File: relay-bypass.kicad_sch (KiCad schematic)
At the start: 39 parts, among them J2 8, K1 IM05JR, Q1 DMN62D0U-7, U1 STM32C011F4Ux

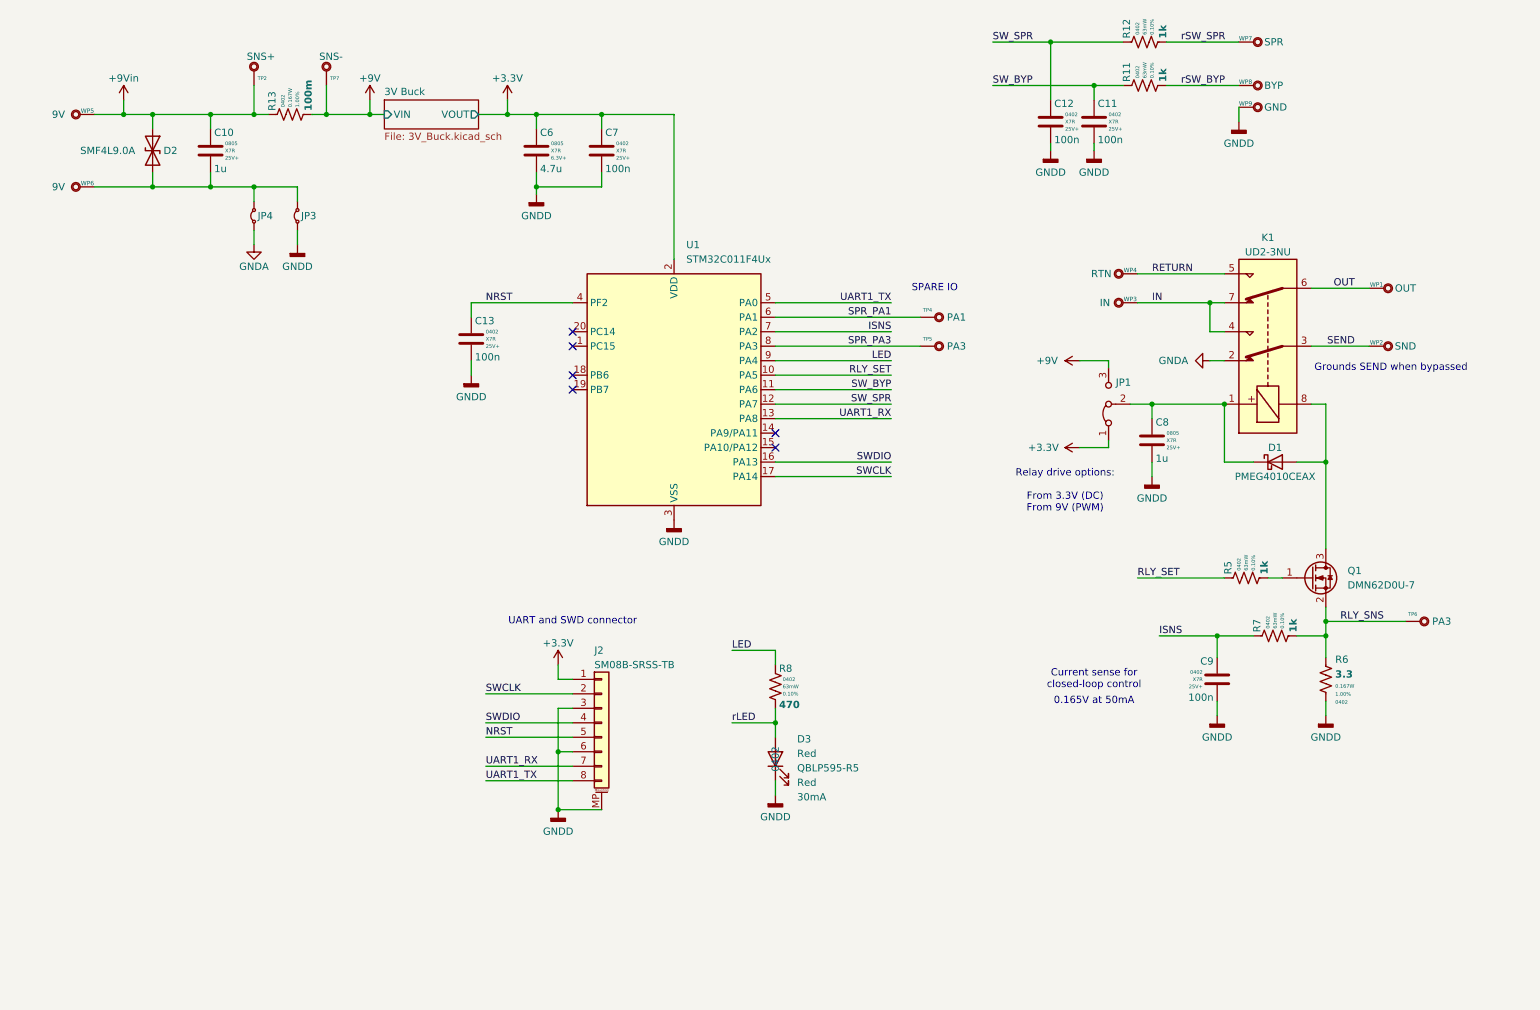
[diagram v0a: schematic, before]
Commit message: Added audio jacks based on recent decision
Decided to make this a board that mounts to audio jacks on top face of a 125B enclosure. May also work for 1590B, TBD. Made most of the schematic changes.
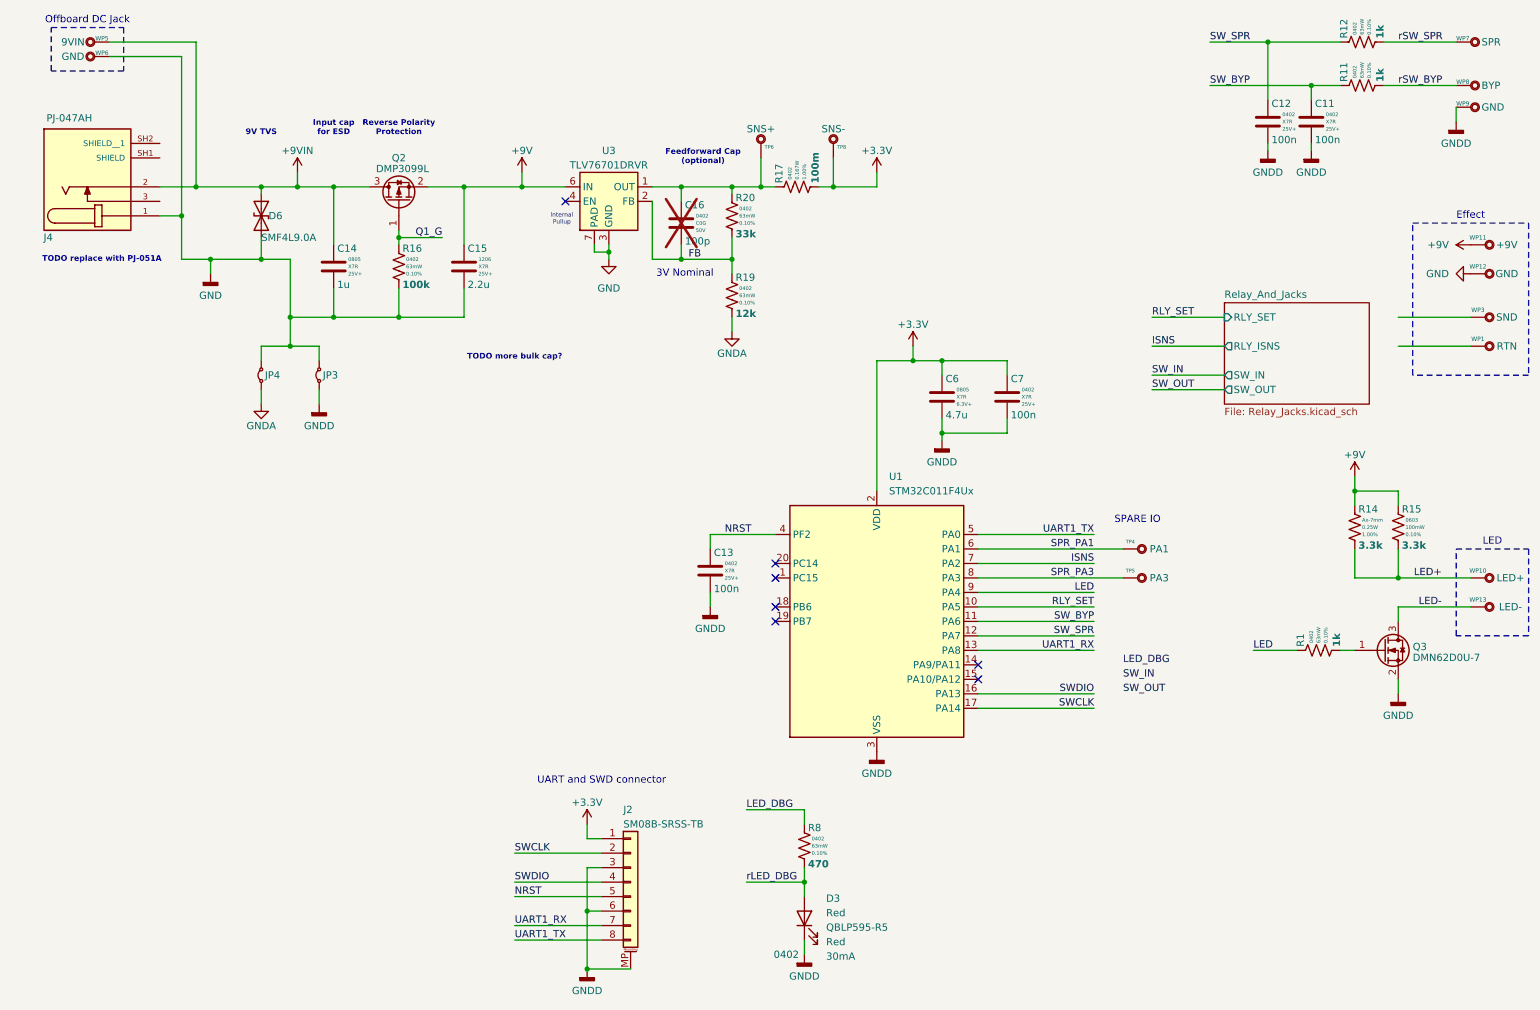
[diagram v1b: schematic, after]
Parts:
- removed C10, C8: 1u, Capacitor_SMD:C_0805_2012Metric, symbol #gplm:cap/CAP-4105-001U
- removed C9: 100n, Capacitor_SMD:C_0402_1005Metric, symbol #gplm:cap/CAP-4103-100N
- removed D1: PMEG4010CEAX, Diode_SMD:D_SOD-323, symbol #gplm:dio/DIO-2001-0001
- removed D2: SMF4L9.0A, Diode_SMD:D_SOD-123F, symbol #gplm:tvs/TVS-1001-09B0
- removed JP1: Jumper_3_Bridged12, Jumper:SolderJumper-3_P1.3mm_Bridged12_Pad1.0x1.5mm, symbol #gplm:art/ART-1000-3001
- removed K1: IM05JR, g-rly:UD23NU, symbol #gplm:rly/RLY-0004-0103
- removed Q1: DMN62D0U-7, Package_TO_SOT_SMD:SOT-23, symbol #gplm:fet/XTR-1003-0001
- removed R13: 100m, Resistor_SMD:R_0402_1005Metric, symbol #gplm:res/RES-2003-0R10
- removed R5, R7: 1k, Resistor_SMD:R_0402_1005Metric, symbol #gplm:res/RES-2002-001K
- removed R6: 3.3, Resistor_SMD:R_0402_1005Metric, symbol #gplm:res/RES-2003-03R3
- removed TP2: SNS+, g-art:TestPoint_PTH_H1.02mm_NoOutline, symbol #gplm:art/ART-0000-N102
- removed TP7: SNS-, g-art:TestPoint_PTH_H1.02mm_NoOutline, symbol #gplm:art/ART-0000-N102
- removed WP2: SND, g-art:WirePad_H0.95mm_22-24AWG, symbol #gplm:art/ART-1001-0P95
- removed WP4: RTN, g-art:WirePad_H0.95mm_22-24AWG, symbol #gplm:art/ART-1001-0P95
- added C14: 1u, Capacitor_SMD:C_0805_2012Metric, symbol #gplm:cap/CAP-4105-001U
- added C15: 2.2u, Capacitor_SMD:C_1206_3216Metric, symbol #gplm:cap/CAP-4106-02U2
- added C16: 100p, Capacitor_SMD:C_0402_1005Metric, symbol #gplm:cap/CAP-4001-0101
- added D6: SMF4L9.0A, Diode_SMD:D_SOD-123F, symbol #gplm:tvs/TVS-1001-09B0
- added J4: 1, g-con:BarrelJack_CUI_PJ-047AH, symbol #gplm:con/CON-4001-0001
- added Q2: DMP3099L, Package_TO_SOT_SMD:SOT-23, symbol #gplm:fet/XTR-1001-0001
- added Q3: DMN62D0U-7, Package_TO_SOT_SMD:SOT-23, symbol #gplm:fet/XTR-1003-0001
- added R1: 1k, Resistor_SMD:R_0402_1005Metric, symbol #gplm:res/RES-2002-001K
- added R14: 3.3k, g-res:R_Axial_DIN0207_L6.3mm_D2.5mm_P7.5mm_Horizontal, symbol #gplm:res/RES-1001-3301
- added R15: 3.3k, Resistor_SMD:R_0603_1608Metric, symbol #gplm:res/RES-2001-03K3
- added R16: 100k, Resistor_SMD:R_0402_1005Metric, symbol #gplm:res/RES-2002-100K
- added R17: 100m, Resistor_SMD:R_0402_1005Metric, symbol #gplm:res/RES-2003-0R10
- added R19: 12k, Resistor_SMD:R_0402_1005Metric, symbol #gplm:res/RES-2002-012K
- added R20: 33k, Resistor_SMD:R_0402_1005Metric, symbol #gplm:res/RES-2002-033K
- added TP8: SNS-, g-art:TestPoint_PTH_H1.02mm_NoOutline, symbol #gplm:art/ART-0000-N102
- added U3: TLV76701DRVR, Package_SON:WSON-6-1EP_2x2mm_P0.65mm_EP1x1.6mm, symbol #gplm:reg/REG-1005-0001
- added WP10: LED+, g-art:WirePad_H0.95mm_22-24AWG, symbol #gplm:art/ART-1001-0P95
- added WP11: +9V, g-art:WirePad_H0.95mm_22-24AWG, symbol #gplm:art/ART-1001-0P95
- added WP12: GND, g-art:WirePad_H0.95mm_22-24AWG, symbol #gplm:art/ART-1001-0P95
- added WP13: LED-, g-art:WirePad_H0.95mm_22-24AWG, symbol #gplm:art/ART-1001-0P95
- TP6: value PA3 -> SNS+
- WP1: value OUT -> RTN
- WP3: value IN -> SND
- WP5: value 9V -> 9VIN
- WP6: value 9V -> GND
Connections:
- net +3.3V: now also R17.2, TP8.1
- net +9V: now also C15.1, Q2.2 (S), R14.1, R15.1, U3.6 (IN), WP11.1
- net GNDA: now also R19.2
- net GNDD: now also Q3.2 (S)
- net LED: now also R1.1; no longer R8.1
- net GND: now reaches JP3.2 (B), JP4.2 (B), WP6.1
- net GND: now also C14.2, C15.2, D6.2 (A2), J4.1, R16.2, U3.3 (GND), U3.5 (GND), U3.7 (PAD), WP12.1
- net +9Vin renamed +9VIN
- net +9VIN: now also C14.1, D6.1 (A1), J4.2, Q2.3 (D)
- net IN: no longer names the net of WP3.1
- net OUT: no longer names the net of WP1.1
- net RLY_SNS: no longer names the net of TP6.1
- net RLY_SNS: now also C16.1, R17.1, R20.1, U3.1 (OUT)
- net rLED renamed rLED_DBG
- new net: Q3.1 (G), R1.2
- new net FB: C16.2, R19.1, R20.2, U3.2 (FB)
- new net LED+: R14.2, R15.2, WP10.1
- new net LED-: Q3.3 (D), WP13.1
- new net LED_DBG: R8.1
- new net Q1_G: Q2.1 (G), R16.1
- no-connect marks 6 -> 7
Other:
- removed sheet 3V Buck
- added sheet Relay_And_Jacks (Relay_Jacks.kicad_sch)
- note added: "3V Nominal"
- note added: "9V TVS"
- note added: "Effect"
- note added: "Feedforward Cap (optional)"
- note added: "Input cap for ESD"
- note added: "Internal Pullup"
- note added: "LED"
- note added: "Offboard DC Jack"
- note added: "Reverse Polarity Protection"
- note added: "TODO more bulk cap?"
- note added: "TODO replace with PJ-051A"
- note removed: "0.165V at 50mA"
- note removed: "Current sense for closed-loop control"
- note removed: "Grounds SEND when bypassed"
- note removed: "Relay drive options: From 3.3V (DC) From 9V (PWM)"
- moved on the sheet: C11, C12, C13, C6, C7, D3, J2, JP3, JP4, R11, R12, R8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

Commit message: Schematic done?
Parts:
- removed C16: 100p, Capacitor_SMD:C_0402_1005Metric, symbol #gplm:cap/CAP-4001-0101
- removed C6: 4.7u, Capacitor_SMD:C_0805_2012Metric, symbol #gplm:cap/CAP-4110-04U7
- removed J4: 1, g-con:BarrelJack_CUI_PJ-047AH, symbol #gplm:con/CON-4001-0001
- removed R17: 100m, Resistor_SMD:R_0402_1005Metric, symbol #gplm:res/RES-2003-0R10
- removed TP6: SNS+, g-art:TestPoint_PTH_H1.02mm_NoOutline, symbol #gplm:art/ART-0000-N102
- removed TP8: SNS-, g-art:TestPoint_PTH_H1.02mm_NoOutline, symbol #gplm:art/ART-0000-N102
- added C1: 1u, Capacitor_SMD:C_0603_1608Metric, symbol #gplm:cap/CAP-4107-001U
- added C10: 10p, Capacitor_SMD:C_0402_1005Metric, symbol #gplm:cap/CAP-4001-0100
- added C2: 220n, Capacitor_SMD:C_0402_1005Metric, symbol #gplm:cap/CAP-4103-220N
- added C3: 10n, Capacitor_SMD:C_0402_1005Metric, symbol #gplm:cap/CAP-4103-010N
- added C4: 22n, Capacitor_SMD:C_0402_1005Metric, symbol #gplm:cap/CAP-4103-022N
- added C5, C6: 47u, Capacitor_SMD:CP_Elec_6.3x5.8, symbol #gplm:cap/CAP-3005-047U
- added J4: 3, g-con:BarrelJack_CUI_PJ-051A, symbol #gplm:con/CON-4002-0001
- added TP1: PA3, g-art:TestPoint_PTH_H1.02mm_NoOutline, symbol #gplm:art/ART-0000-N102
- TP4: value PA1 -> PA8
- WP7: value SPR -> PA7
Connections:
- net +3.3V: now also R20.1, U3.1 (OUT), C1.1, C10.1, C2.1, C3.1, C4.1, C5.1
- net +9V: now also C6.1
- net +9VIN: now also J4.2
- net FB: now also C10.2
- net GND: now also J4.1, J4.SH1 (SHIELD), J4.SH2 (SHIELD__1); no longer C15.2, R16.2, U3.3 (GND), U3.5 (GND), U3.7 (PAD), WP12.1
- net GNDA: now also R16.2, WP12.1, C6.2; no longer R19.2
- net GNDD: now also C15.2, R19.2, U3.3 (GND), U3.5 (GND), U3.7 (PAD), C1.2, C2.2, C3.2, C4.2, C5.2
- net LED_DBG: now also U1.14 (PA9/PA11)
- net SW_IN: now also U1.18 (PB6)
- net SW_OUT: now also U1.19 (PB7)
- net UART1_RX: now also U1.6 (PA1); no longer U1.13 (PA8)
- net Relay_And_Jacks/RETURN: now reaches WP1.1
- net MUTE: now reaches U1.15 (PA10/PA12)
- net CLK_IN: now reaches U1.20 (PC14)
- net CLK_IN: now also TP1.1
- net Relay_And_Jacks/SEND: now reaches WP3.1
- net LED renamed LED_EXT
- net SPR_PA1 renamed SPR_PA8
- net SPR_PA8: now also U1.13 (PA8); no longer U1.6 (PA1)
- no-connect marks 7 -> 3
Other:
- sheet Relay_And_Jacks ports: added MUTE, RETURN, SEND; removed none
- note added: "Footswitch"
- note added: "Onboard DC Jack"
- note added: "Output Capacitance Requirements: 1uF < Cout < 220uF 2mOhm < ESR < 500mOhm Total capacitance: ~50u ESR: ~4mOhm"
- note added: "Spare MCU Pins"
- note removed: "TODO more bulk cap?"
- note removed: "TODO replace with PJ-051A"
- moved on the sheet: C11, C12, C13, C14, C15, C7, JP3, JP4, Q3, R1, R11, R12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

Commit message: Committing uncommitted work, not sure what it was
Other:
- note added: "TODO change to LDO that's stable w/ low ESR?"
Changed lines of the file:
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@@
+		)
+	)
+	(text "TODO change to LDO that's stable w/ low ESR?"
+		(exclude_from_sim no)
+		(at 131.445 29.21 0)
+		(effects
+			(font
+				(size 1.27 1.27)
+				(color 132 0 0 1)
+			)
 		)
 	)
